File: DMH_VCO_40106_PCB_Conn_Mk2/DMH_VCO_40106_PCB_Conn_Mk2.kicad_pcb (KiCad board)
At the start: 2 copper layers, 98 x 62 mm, 11 parts, among them J1 TS_Jack_6.35mm_Sw, J150 Conn_01x12, J2 TS_Jack_6.35mm_Sw, J200 IDC_02x05, J3 TS_Jack_6.35mm_Sw, J4 TS_Jack_6.35mm_Sw, J5 TS_Jack_6.35mm_Sw, J6 TS_Jack_6.35mm_Sw, J7 TS_Jack_6.35mm_Sw, J8 TS_Jack_6.35mm_Sw, J9 TS_Jack_6.35mm_Sw

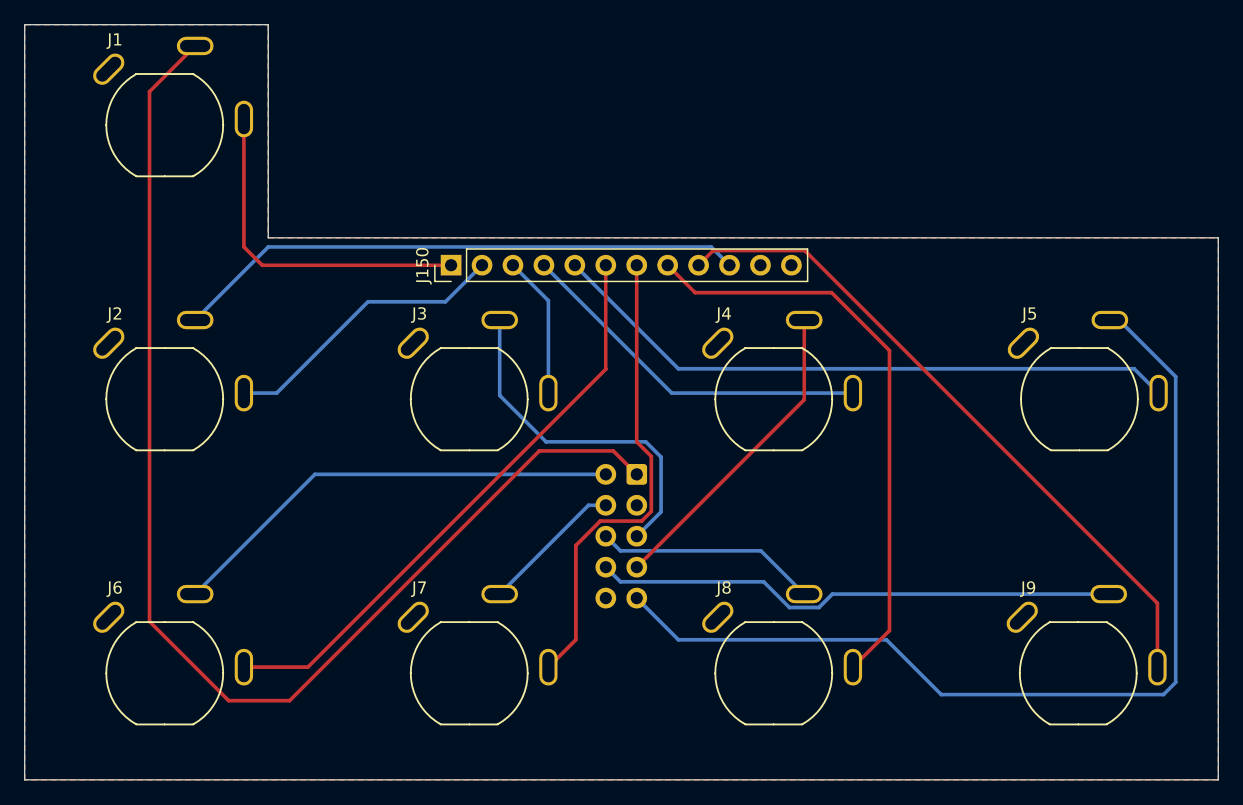
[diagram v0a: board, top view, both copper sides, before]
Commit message: Routed Mk2 conn PCB
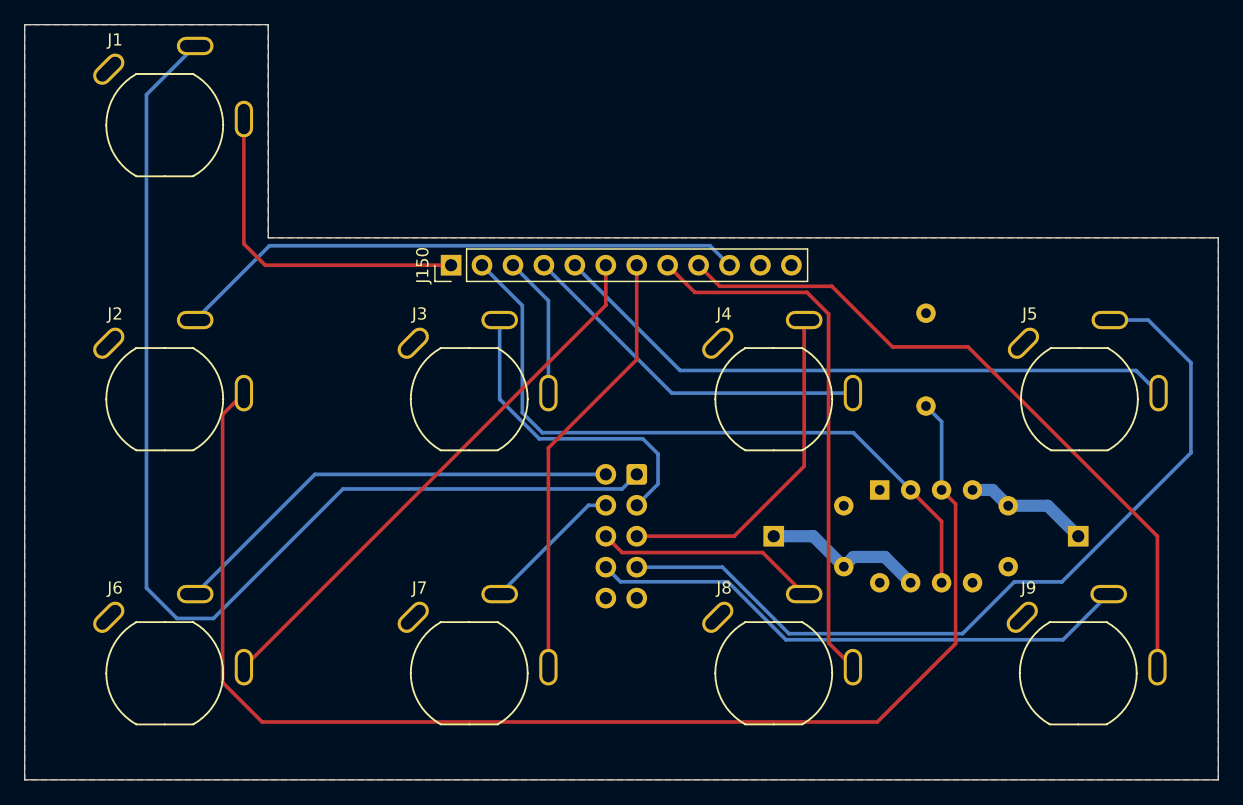
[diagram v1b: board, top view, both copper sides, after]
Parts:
- added C21: 100nF, Capacitor_THT:C_Disc_D4.3mm_W1.9mm_P5.00mm, B.Cu at (118.2, 220.0)
- added C22: 100nF, Capacitor_THT:C_Disc_D4.3mm_W1.9mm_P5.00mm, B.Cu at (131.8, 215.0)
- added J11: Conn_01x01, Connector_PinHeader_2.54mm:PinHeader_1x01_P2.54mm_Vertical, B.Cu at (112.5, 217.5)
- added J12: Conn_01x01, Connector_PinHeader_2.54mm:PinHeader_1x01_P2.54mm_Vertical, B.Cu at (137.5, 217.5)
- added R75: 5M, Resistor_THT:R_Axial_DIN0207_L6.3mm_D2.5mm_P7.62mm_Horizontal, B.Cu at (125.0, 199.2)
- added U7: TL071, Package_DIP:DIP-8_W7.62mm_Socket, B.Cu at (121.2, 213.7)
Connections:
- J2 pad T: Net-(J150-Pin_2) -> Net-(U7-+)
- J200 pad 10: unconnected-(J200-Pin_10-Pad10) -> GND
- J200 pad 2: unconnected-(J200-Pin_2-Pad2) -> Net-(J200-Pin_2)
- J200 pad 5: Net-(J200-Pin_5) -> GND
- J3 pad TN: Net-(J200-Pin_3) -> Net-(J200-Pin_2)
- J4 pad TN: Net-(J200-Pin_4) -> Net-(J200-Pin_3)
- J5 pad TN: Net-(J200-Pin_5) -> Net-(J200-Pin_4)
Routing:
- net Net-(U7-+): track 0.00 -> 109.2 mm
- net Net-(J200-Pin_5): track 80.4 -> 0.00 mm
- net Net-(J200-Pin_4): track 26.0 -> 69.4 mm
- net Net-(J150-Pin_2): track 24.2 -> 56.9 mm
- net Net-(J200-Pin_2): track 0.00 -> 26.3 mm
- net +12V: track 0.00 -> 13.5 mm
- net -12V: track 0.00 -> 10.3 mm
- net Net-(J200-Pin_1): track 100.8 -> 92.3 mm
- net Net-(J150-Pin_8): track 48.4 -> 44.7 mm
- net Net-(J150-Pin_6): track 48.4 -> 45.3 mm
- net Net-(J150-Pin_7): track 39.0 -> 36.0 mm
- net Net-(J150-Pin_9): track 55.4 -> 57.6 mm
- net Net-(J200-Pin_9): track 43.1 -> 45.3 mm
- net Net-(J200-Pin_3): track 28.9 -> 28.1 mm
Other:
- board text added: "Mk2.0 - January 2025"
- board text removed: "Mk1.1 - September 2024"

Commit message: Changed buffer resistor to 10M
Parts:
- R75: value 5M -> 10M
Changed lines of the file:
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@@
 		)
 		(property ki_fp_filters "Jack*")
-		(sheetname "Inpus and Outputs")
+		(sheetname "/Inpus and Outputs/")
 		(sheetfile "Inputs_and_Outputs.kicad_sch")
 		(attr through_hole)
@@
 		)
 		(property ki_fp_filters "Jack*")
-		(sheetname "Inpus and Outputs")
+		(sheetname "/Inpus and Outputs/")
 		(sheetfile "Inputs_and_Outputs.kicad_sch")
 		(attr through_hole)
@@
 		)
 		(property ki_fp_filters "Jack*")
-		(sheetname "Inpus and Outputs")
+		(sheetname "/Inpus and Outputs/")
 		(sheetfile "Inputs_and_Outputs.kicad_sch")
 		(attr through_hole)
@@
 		)
 		(property ki_fp_filters "Jack*")
-		(sheetname "Inpus and Outputs")
+		(sheetname "/Inpus and Outputs/")
 		(sheetfile "Inputs_and_Outputs.kicad_sch")
 		(attr through_hole)
@@
 		)
 		(property ki_fp_filters "Jack*")
-		(sheetname "Inpus and Outputs")
+		(sheetname "/Inpus and Outputs/")
 		(sheetfile "Inputs_and_Outputs.kicad_sch")
 		(attr through_hole)
@@
 		)
 		(property ki_fp_filters "Jack*")
-		(sheetname "Inpus and Outputs")
+		(sheetname "/Inpus and Outputs/")
 		(sheetfile "Inputs_and_Outputs.kicad_sch")
 		(attr through_hole)
@@
 		)
 		(property ki_fp_filters "Jack*")
-		(sheetname "Inpus and Outputs")
+		(sheetname "/Inpus and Outputs/")
 		(sheetfile "Inputs_and_Outputs.kicad_sch")
 		(attr through_hole)
@@
 		)
 		(property ki_fp_filters "Jack*")
-		(sheetname "Inpus and Outputs")
+		(sheetname "/Inpus and Outputs/")
 		(sheetfile "Inputs_and_Outputs.kicad_sch")
 		(attr through_hole)
@@
 		)
 		(property ki_fp_filters "Jack*")
-		(sheetname "Inpus and Outputs")
+		(sheetname "/Inpus and Outputs/")
 		(sheetfile "Inputs_and_Outputs.kicad_sch")
 		(attr through_hole)
@@
 		)
 		(property ki_fp_filters "Connector*:*_1x??_*")
-		(sheetname "Inpus and Outputs")
+		(sheetname "/Inpus and Outputs/")
 		(sheetfile "Inputs_and_Outputs.kicad_sch")
 		(attr through_hole)
@@
 		)
 		(property ki_fp_filters "C_*")
-		(sheetname "Inpus and Outputs")
+		(sheetname "/Inpus and Outputs/")
 		(sheetfile "Inputs_and_Outputs.kicad_sch")
 		(attr through_hole)
@@
 		)
 		(property ki_fp_filters "Connector*:*_1x??_*")
-		(sheetname "Inpus and Outputs")
+		(sheetname "/Inpus and Outputs/")
 		(sheetfile "Inputs_and_Outputs.kicad_sch")
 		(attr through_hole)
@@
 		)
 		(property ki_fp_filters "Connector*:*_1x??_*")
-		(sheetname "Inpus and Outputs")
+		(sheetname "/Inpus and Outputs/")
 		(sheetfile "Inputs_and_Outputs.kicad_sch")
 		(attr through_hole)
@@
 		)
 		(property ki_fp_filters "SOIC*3.9x4.9mm*P1.27mm* DIP*W7.62mm* TSSOP*3x3mm*P0.65mm*")
-		(sheetname "Inpus and Outputs")
+		(sheetname "/Inpus and Outputs/")
 		(sheetfile "Inputs_and_Outputs.kicad_sch")
 		(attr through_hole)
@@
 		)
 		(property ki_fp_filters "Connector*:*_2x??_*")
-		(sheetname "Inpus and Outputs")
+		(sheetname "/Inpus and Outputs/")
 		(sheetfile "Inputs_and_Outputs.kicad_sch")
 		(attr through_hole)
@@
 		)
 		(property ki_fp_filters "C_*")
-		(sheetname "Inpus and Outputs")
+		(sheetname "/Inpus and Outputs/")
 		(sheetfile "Inputs_and_Outputs.kicad_sch")
 		(attr through_hole)
@@
 			)
 		)
-		(property "Value" "5M"
+		(property "Value" "10M"
 			(at 3.81 0 90)
 			(layer "B.SilkS")
@@
 		)
 		(property ki_fp_filters "R_*")
-		(sheetname "Inpus and Outputs")
+		(sheetname "/Inpus and Outputs/")
 		(sheetfile "Inputs_and_Outputs.kicad_sch")
 		(attr through_hole)

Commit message: Generated PCB Conn Mk2 Gerbers
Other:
- board text added: "Mk2.0 - March 2025"
- board text removed: "Mk2.0 - January 2025"
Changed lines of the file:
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@@
 			(drillshape 0)
 			(scaleselection 1)
-			(outputdirectory "")
+			(outputdirectory "Gerbers/")
 		)
 	)
@@
 		(layer "User.9")
 	)
-	(gr_text "Mk2.0 - January 2025"
+	(gr_text "Mk2.0 - March 2025"
 		(at 138.25 235.5 0)
 		(layer "B.SilkS")
